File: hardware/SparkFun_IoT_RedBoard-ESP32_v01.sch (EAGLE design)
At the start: 113 parts, among them J1 5.5x2.1mm Barrel, J13 QWIIC_RIGHT_ANGLE, J15 MICRO-SD-PUSH-PUSH-EXT-PIN, J2 USB C, J3 USB_SOLDER_PADS, J5 M10NO_SILK, Q1 MBT3904DW1T1, Q11 20V/4.2A/52mΩ/1.4W, Q13 20V/4.2A/52mΩ/1.4W, Q3 20V/4.2A/52mΩ/1.4W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

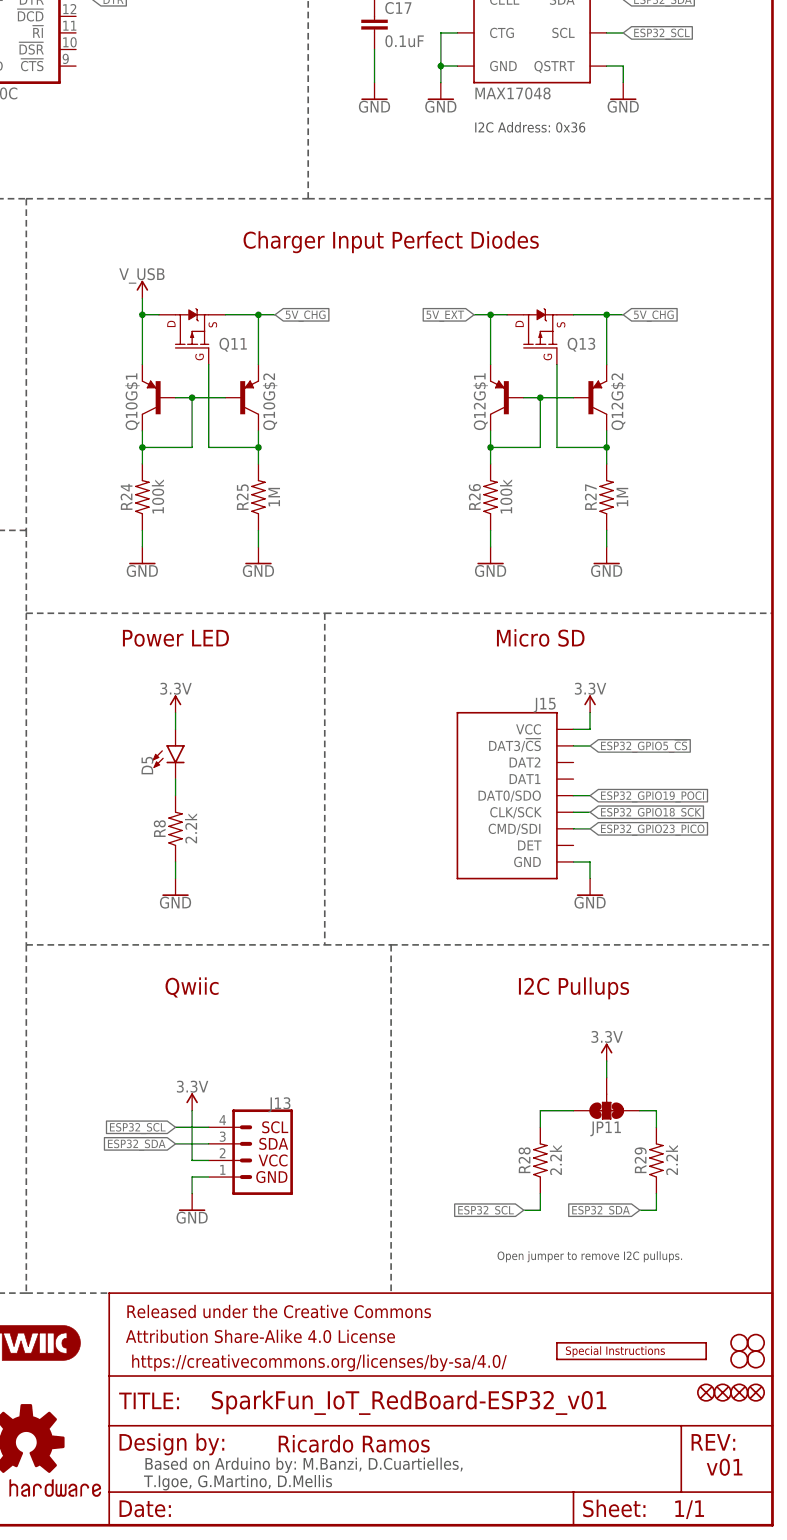
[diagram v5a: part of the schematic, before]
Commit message: Add "revised by" and change version number
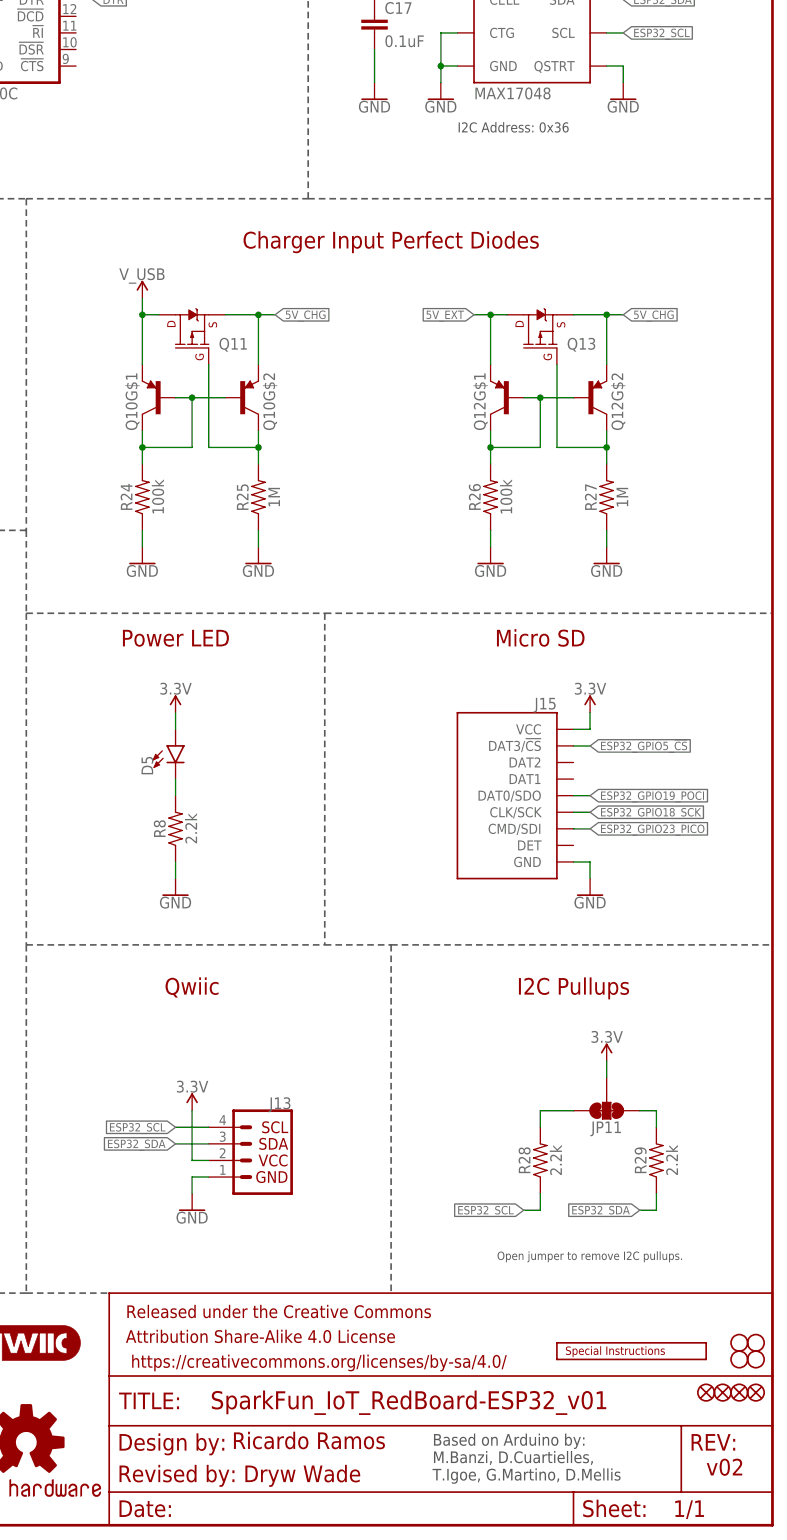
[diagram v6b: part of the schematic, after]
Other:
- note added: "Revised by: Dryw Wade"
- note added: "v02"
- note removed: "v01"
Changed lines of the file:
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@@
 <sheet>
 <plain>
-<text x="335.534" y="5.842" size="1.778" layer="97" font="vector">Based on Arduino by: M.Banzi, D.Cuartielles,
+<text x="379.73" y="6.858" size="1.778" layer="97" font="vector">Based on Arduino by:
+M.Banzi, D.Cuartielles,
 T.Igoe, G.Martino, D.Mellis</text>
-<text x="355.854" y="11.176" size="2.54" layer="94" font="vector">Ricardo Ramos</text>
-<text x="421.64" y="7.62" size="2.54" layer="94" font="vector">v01</text>
+<text x="348.996" y="11.684" size="2.54" layer="94" font="vector">Ricardo Ramos</text>
+<text x="421.64" y="7.62" size="2.54" layer="94" font="vector">v02</text>
 <text x="254" y="254" size="1.778" layer="97" font="vector">This is the penny-in-the-fuse jumper.
 Close only if you know what you're doing.</text>
@@
 <wire x1="243.84" y1="35.56" x2="243.84" y2="0" width="0.254" layer="97" style="longdash"/>
 <text x="152.4" y="269.24" size="1.778" layer="94" font="vector" ratio="11" align="bottom-center">Inputs are NOT 5V tolerant.</text>
-<text x="386.08" y="213.36" size="1.524" layer="97">I2C Address: 0x36</text>
+<text x="383.54" y="213.36" size="1.524" layer="97" font="vector">I2C Address: 0x36</text>
 <text x="50.8" y="96.52" size="1.27" layer="97" font="vector" align="bottom-center">Open jumpers to isolate GPIO13
 and GPIO14 from the JTAG header</text>
@@
 board current on J14</text>
 <text x="403.86" y="40.64" size="1.27" layer="97" font="vector" align="bottom-center">Open jumper to remove I2C pullups.</text>
+<text x="331.47" y="6.604" size="2.54" layer="94" font="vector">Revised by: Dryw Wade</text>
 </plain>
 <instances>

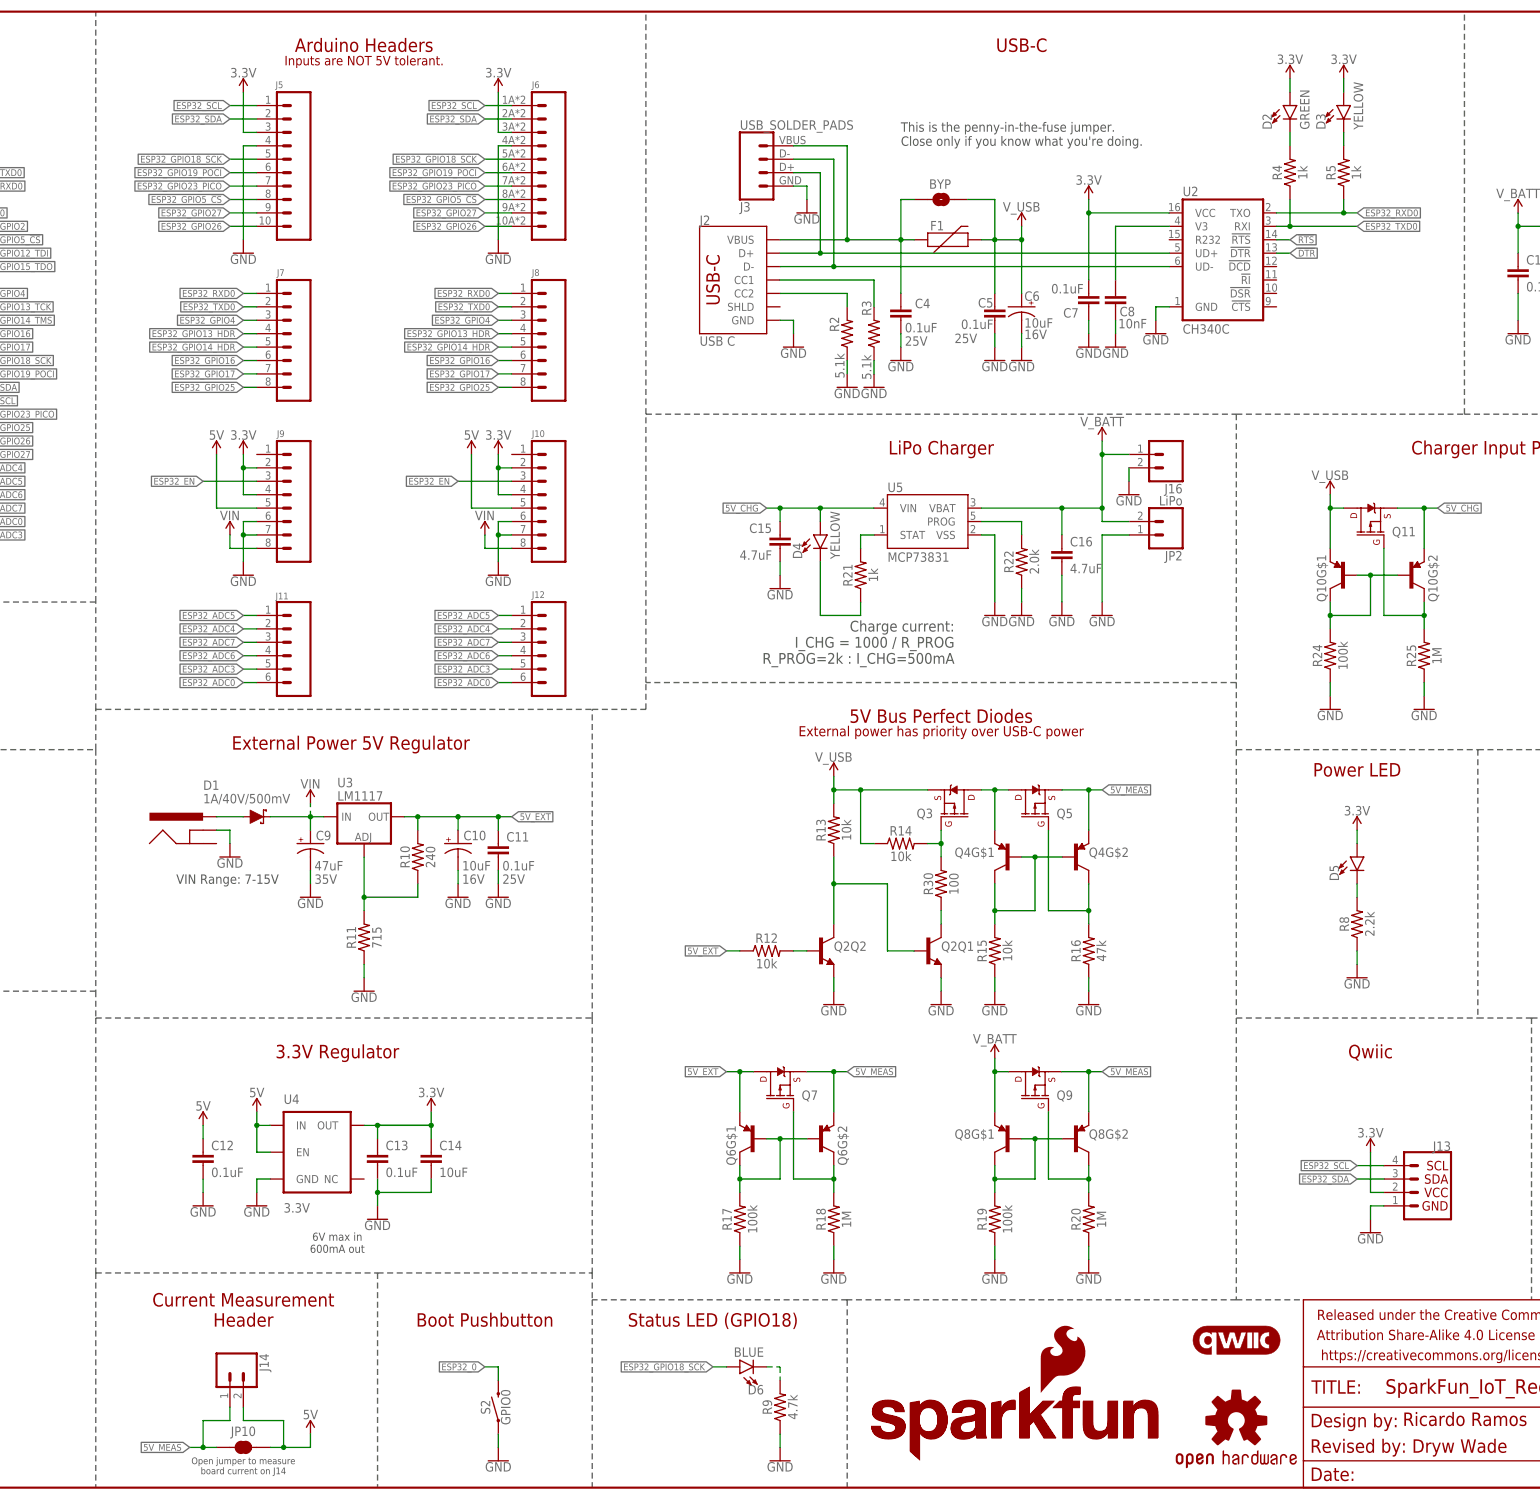
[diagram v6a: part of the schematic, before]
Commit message: Change PTC Fuse
Reduce current rating of PTC
Move PTC to 5V_MEAS to protect all power inputs rather than just USB
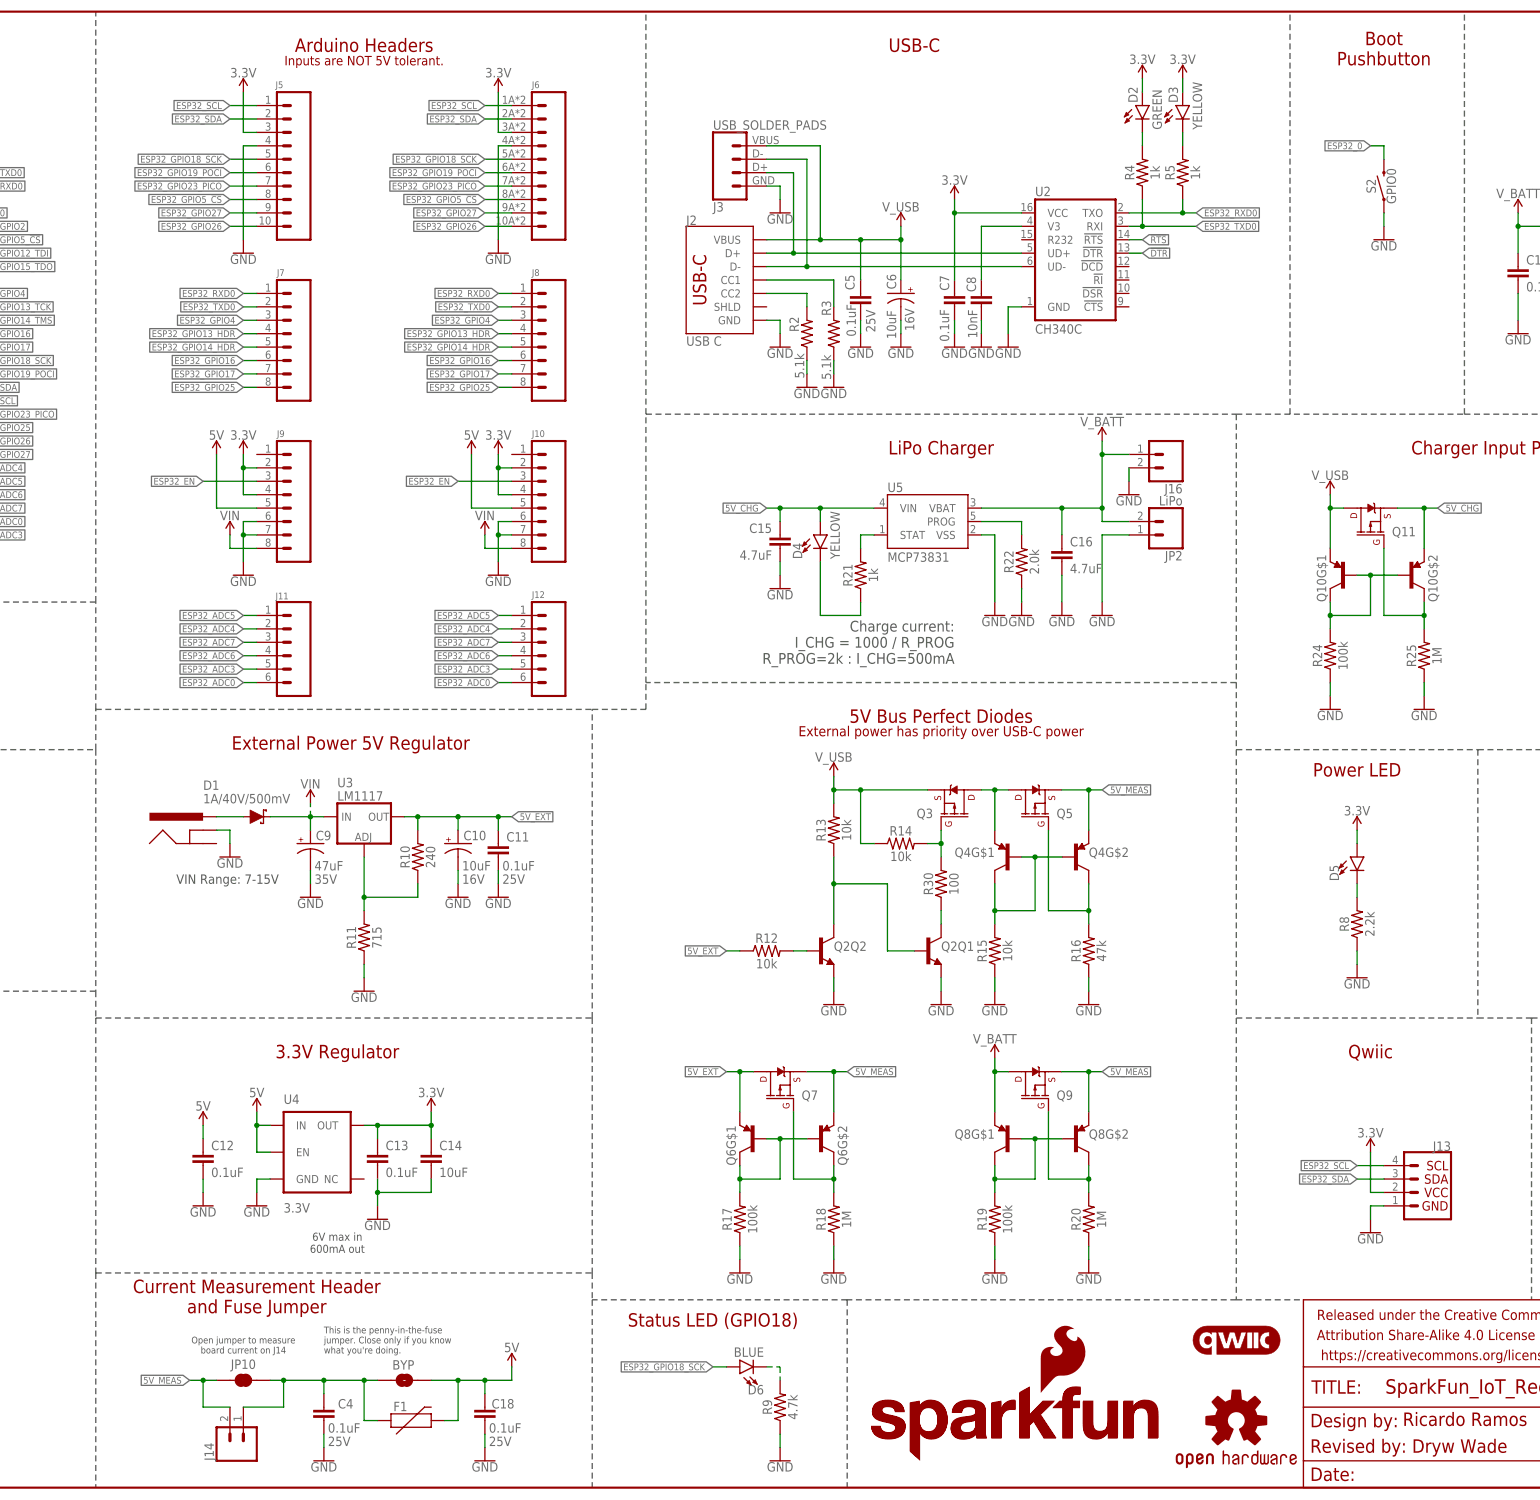
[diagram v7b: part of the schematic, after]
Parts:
- added C18: 0.1uF, SparkFun-Capacitors:0.1UF-0603-25V-(+80/-20%)
- F1: value 6V/2A -> 6V/0.75A; device SparkFun-Fuses:PPTC_6V2A -> SparkFun-Fuses:PPTC_0.75A
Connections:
- removed net VBUS: BYP.1, C4.1, F1.1, J2.VBUS, J3.1
- new net N$19: BYP.1, C4.1, F1.1, J14.1, JP10.2
- net 5V: now also BYP.2, C18.1, F1.2; no longer J14.2, JP10.2
- net 5V_MEAS: now also J14.2; no longer J14.1
- net GND: now also C18.2
- net V_USB: now also J2.VBUS, J3.1; no longer BYP.2, F1.2
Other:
- note added: "Current Measurement Header and Fuse Jumper"
- note removed: "Current Measurement Header"
- moved on the sheet: BYP, C4, C5, C6, C7, C8, D2, D3, F1, J14, J2, J3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
